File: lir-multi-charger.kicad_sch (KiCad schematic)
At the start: 2 parts, among them J1 Conn_01x02_Female

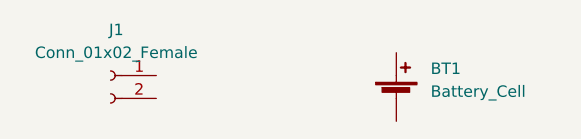
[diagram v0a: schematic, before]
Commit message: finished CR2450 battery holder footprint
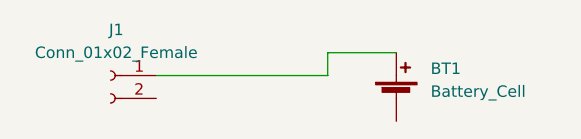
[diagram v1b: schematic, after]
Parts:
- BT1: footprint Battery:BatteryHolder_ComfortableElectronic_CH273-2450_1x2450 -> Battery_Coin_SMD:CR2450
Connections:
- net at BT1.1 (+): now also J1.1 (Pin_1)
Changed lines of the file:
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@@
 (kicad_sch (version 20211123) (generator eeschema)
   (paper "A4")
+  (wire (pts (xy 52.07 102.87) (xy 59.69 102.87))
+    (stroke (width 0) (type default) (color 0 0 0 0))
+  )
+  (wire (pts (xy 52.07 105.41) (xy 52.07 102.87))
+    (stroke (width 0) (type default) (color 0 0 0 0))
+  )
+  (wire (pts (xy 33.02 105.41) (xy 52.07 105.41))
+    (stroke (width 0) (type default) (color 0 0 0 0))
+  )
   (symbol (lib_id "Device:Battery_Cell") (at 59.69 107.95 0) (unit 1)
     (in_bom yes) (on_board yes) (fields_autoplaced)
@@
       (effects (font (size 1.27 1.27)) (justify left))
     )
-    (property "Footprint" "Battery:BatteryHolder_ComfortableElectronic_CH273-2450_1x2450" (id 2) (at 59.69 106.426 90)
+    (property "Footprint" "Battery_Coin_SMD:CR2450" (id 2) (at 59.69 106.426 90)
       (effects (font (size 1.27 1.27)) hide)
     )
@@
   (symbol_instances
     (path "/6a0c578b-7a8f-4b47-bae2-b91033c942ea"
-      (reference "BT1") (unit 1) (value "Battery_Cell") (footprint "Battery:BatteryHolder_ComfortableElectronic_CH273-2450_1x2450")
+      (reference "BT1") (unit 1) (value "Battery_Cell") (footprint "Battery_Coin_SMD:CR2450")
     )
     (path "/ecc76268-d1b1-479a-a89b-3a5c8226dd54"

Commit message: started charger schematic
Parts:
- removed J1: Conn_01x02_Female, TerminalBlock_4Ucon:TerminalBlock_4Ucon_1x02_P3.50mm_Horizontal, symbol Connector:Conn_01x02_Female
- added BT2: Battery_Cell, Battery_Coin_SMD:CR2032, symbol Device:Battery_Cell
- added BT3: Battery_Cell, Battery_Coin_SMD:CR1220, symbol Device:Battery_Cell
- added D1, D2: D_Schottky, Diode_SMD:D_SOD-123, symbol Device:D_Schottky
- added J1: USB_C_Receptacle_USB2.0, Connector_USB:USB_C_Receptacle_HRO_TYPE-C-31-M-12, symbol Connector:USB_C_Receptacle_USB2.0
- added J2: Conn_01x02_Male, Connector_PinHeader_2.54mm:PinHeader_1x02_P2.54mm_Vertical, symbol Connector:Conn_01x02_Male
- added R1, R2: 5.1K, Resistor_SMD:R_0805_2012Metric_Pad1.20x1.40mm_HandSolder, symbol Device:R
- added U1: TP4056, Package_SO:SOP-8_3.9x4.9mm_P1.27mm, symbol Li_ion_charger:TP4056
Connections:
- new net: D1.1 (K), D2.1 (K)
- new net: D1.2 (A), J2.1 (Pin_1)
- new net: J1.A5 (CC1), R2.1
- new net: D2.2 (A), J1.A4 (VBUS), J1.A9 (VBUS), J1.B4 (VBUS), J1.B9 (VBUS)
- new net: J1.A6 (D+), J1.B6 (D+)
- new net: J1.A7 (D-), J1.B7 (D-)
- new net: J1.B5 (CC2), R1.1
- new net GND: J1.A1 (GND), J1.A12 (GND), J1.B1 (GND), J1.B12 (GND), J2.2 (Pin_2), R1.2, R2.2
- no-connect marks 0 -> 3
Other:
- moved on the sheet: BT1

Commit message: started placing components
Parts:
- added C1, C2, C3, C4: 10uF, Capacitor_SMD:C_0805_2012Metric_Pad1.18x1.45mm_HandSolder, symbol Device:C
- added D3, D5: GREEN, LED_SMD:LED_0805_2012Metric_Pad1.15x1.40mm_HandSolder, symbol Device:LED
- added D4, D6: RED, LED_SMD:LED_0805_2012Metric_Pad1.15x1.40mm_HandSolder, symbol Device:LED
- added R10, R5: 0R, Resistor_SMD:R_0805_2012Metric_Pad1.20x1.40mm_HandSolder, symbol Device:R
- added R11, R6: 320k, Resistor_SMD:R_0805_2012Metric_Pad1.20x1.40mm_HandSolder, symbol Device:R
- added R12, R7: 1R, Resistor_SMD:R_0805_2012Metric_Pad1.20x1.40mm_HandSolder, symbol Device:R
- added R3, R4, R8, R9: 1k, Resistor_SMD:R_0805_2012Metric_Pad1.20x1.40mm_HandSolder, symbol Device:R
- added U2: TP4056, Li-ion-charger:tp4056, symbol Li_ion_charger:TP4056
- U1: footprint Package_SO:SOP-8_3.9x4.9mm_P1.27mm -> Li-ion-charger:tp4056
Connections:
- net GND: now also BT2.2 (-), BT3.2 (-), U1.1 (TEMP), U1.3 (GND), C1.2, C2.2, C3.2, C4.2, R12.2, R7.2, U2.1 (TEMP), U2.3 (GND)
- net VBUS: now reaches D1.1 (K), D2.1 (K)
- net VBUS: now also R10.1, R5.1
- net at BT2.1 (+): now also C4.1, U2.5 (BAT)
- net at BT3.1 (+): now also U1.5 (BAT), C2.1
- net at U1.2 (PROG): now also R6.1
- net at U1.4 (VCC): now also U1.8 (CE), C1.1, D3.2 (A), D4.2 (A), R5.2
- net at U1.6 (/STDBY): now also R4.2
- net at U1.7 (/CHRG): now also R3.2
- new net: D5.1 (K), R9.1
- new net: C3.1, D5.2 (A), D6.2 (A), R10.2, U2.4 (VCC), U2.8 (CE)
- new net: R9.2, U2.6 (/STDBY)
- new net: R11.1, U2.2 (PROG)
- new net: R11.2, R12.1
- new net: R6.2, R7.1
- new net: D4.1 (K), R3.1
- new net: D6.1 (K), R8.1
- new net: D3.1 (K), R4.1
- new net: R8.2, U2.7 (/CHRG)
- no-connect marks 3 -> 5
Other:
- moved on the sheet: BT1, BT2, BT3

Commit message: placing components
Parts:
- added C5, C6: 10uF, Capacitor_SMD:C_0805_2012Metric_Pad1.18x1.45mm_HandSolder, symbol Device:C
- added D7: GREEN, LED_SMD:LED_0805_2012Metric_Pad1.15x1.40mm_HandSolder, symbol Device:LED
- added D8: RED, LED_SMD:LED_0805_2012Metric_Pad1.15x1.40mm_HandSolder, symbol Device:LED
- added R13, R14: 1k, Resistor_SMD:R_0805_2012Metric_Pad1.20x1.40mm_HandSolder, symbol Device:R
- added R15: 0R, Resistor_SMD:R_0805_2012Metric_Pad1.20x1.40mm_HandSolder, symbol Device:R
- added R16: 320k, Resistor_SMD:R_0805_2012Metric_Pad1.20x1.40mm_HandSolder, symbol Device:R
- added R17: 1R, Resistor_SMD:R_0805_2012Metric_Pad1.20x1.40mm_HandSolder, symbol Device:R
- added U3: TP4056, Li-ion-charger:tp4056, symbol Li_ion_charger:TP4056
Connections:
- net GND: now also BT1.2 (-), C5.2, C6.2, R17.2, U3.1 (TEMP), U3.3 (GND)
- net VBUS: now also R15.1
- net at BT1.1 (+): now also C6.1, U3.5 (BAT)
- new net: R16.1, U3.2 (PROG)
- new net: C5.1, D7.2 (A), D8.2 (A), R15.2, U3.4 (VCC), U3.8 (CE)
- new net: R14.2, U3.6 (/STDBY)
- new net: R13.2, U3.7 (/CHRG)
- new net: D8.1 (K), R13.1
- new net: D7.1 (K), R14.1
- new net: R16.2, R17.1
- no-connect marks 5 -> 6
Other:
- moved on the sheet: BT1, BT2, BT3, C1, C2, C3, C4, D3, D4, D5, D6, R10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

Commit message: all components placed
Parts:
- added J3, J4, J5, J6: Conn_01x02_Male, Connector_PinHeader_2.54mm:PinHeader_1x02_P2.54mm_Vertical, symbol Connector:Conn_01x02_Male
- added JP1, JP2, JP3: SolderJumper_2_Bridged, Jumper:SolderJumper-2_P1.3mm_Bridged_RoundedPad1.0x1.5mm, symbol Jumper:SolderJumper_2_Bridged
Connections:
- net at C6.1, U3.5 (BAT): now also J5.1 (Pin_1), JP3.1 (A); no longer BT1.1 (+)
- net at C2.1, U1.5 (BAT): now also J3.1 (Pin_1), JP1.1 (A); no longer BT3.1 (+)
- net at C4.1, U2.5 (BAT): now also J4.1 (Pin_1), JP2.1 (A); no longer BT2.1 (+)
- net at J1.A6 (D+), J1.B6 (D+): now also J6.1 (Pin_1)
- net at J1.A7 (D-), J1.B7 (D-): now also J6.2 (Pin_2)
- new net: BT1.1 (+), J5.2 (Pin_2), JP3.2 (B)
- new net: BT2.1 (+), J4.2 (Pin_2), JP2.2 (B)
- new net: BT3.1 (+), J3.2 (Pin_2), JP1.2 (B)
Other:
- moved on the sheet: BT1, R1, R2

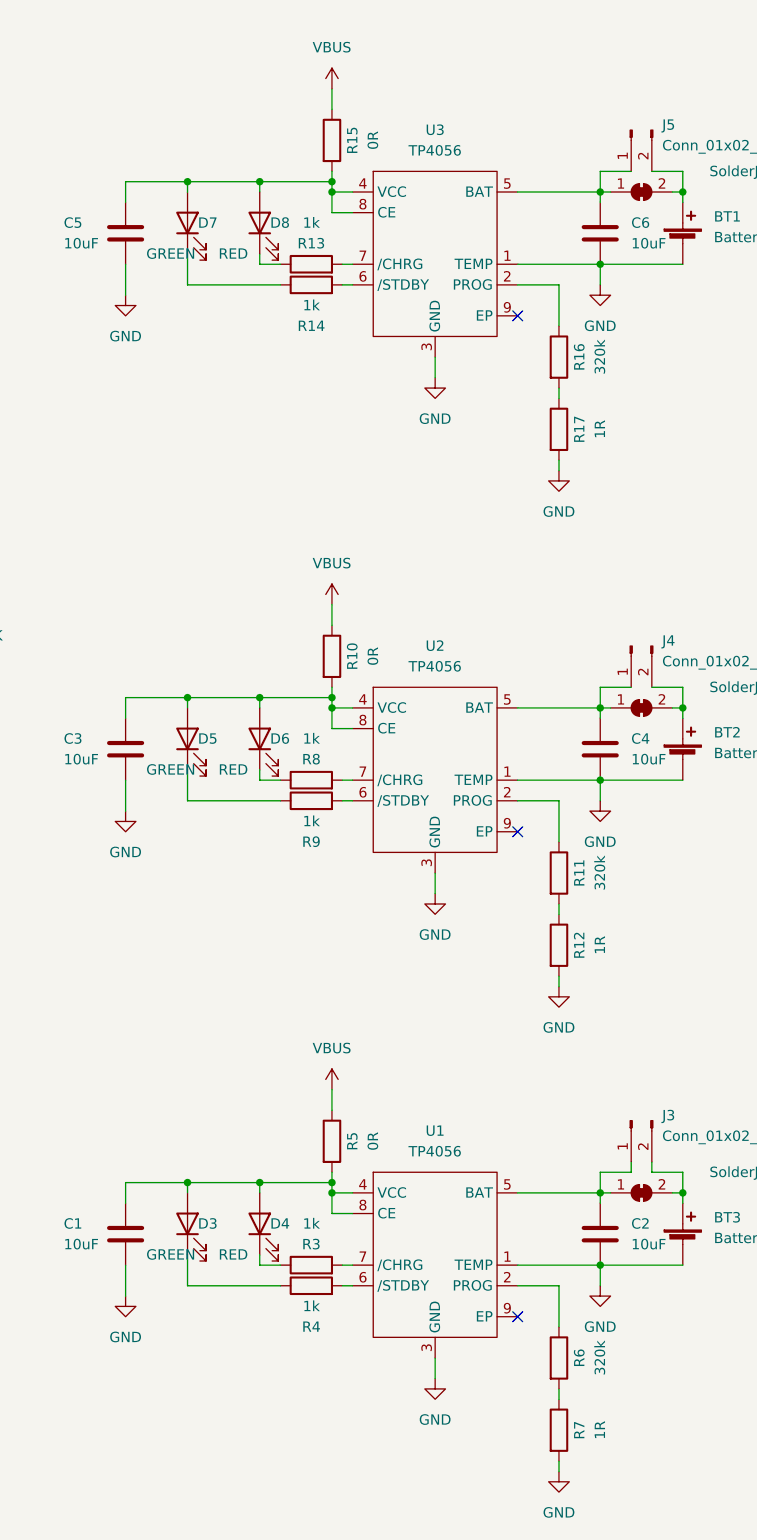
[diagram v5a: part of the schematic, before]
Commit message: changed charger IC
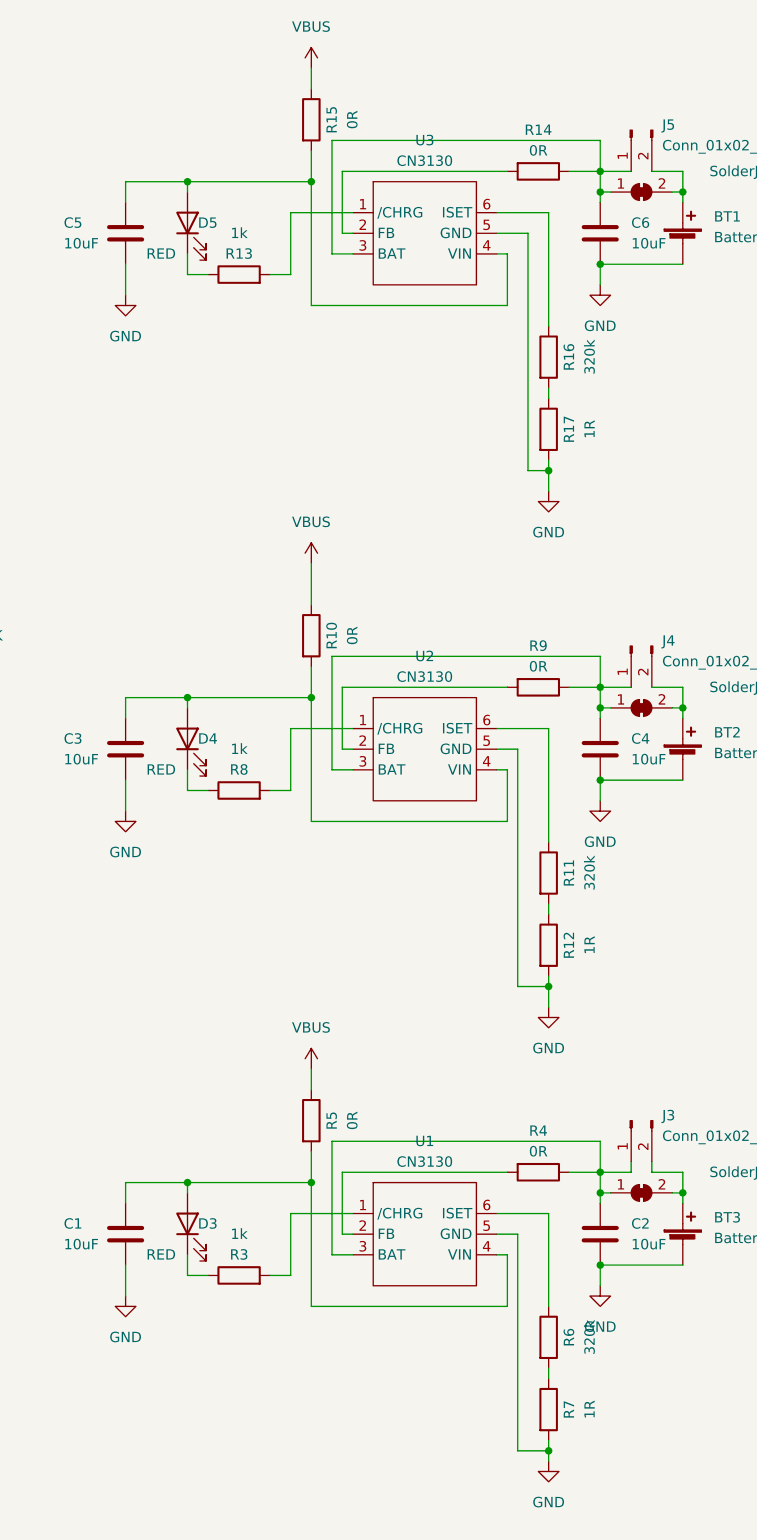
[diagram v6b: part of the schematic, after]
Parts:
- removed D3, D5, D7: GREEN, LED_SMD:LED_0805_2012Metric_Pad1.15x1.40mm_HandSolder, symbol Device:LED
- removed U1, U2, U3: TP4056, Li-ion-charger:tp4056, symbol Li_ion_charger:TP4056
- added U1, U2, U3: CN3130, Package_TO_SOT_SMD:SOT-23-6_Handsoldering, symbol coin-batt-charger:CN3130
- R14, R4, R9: value 1k -> 0R
- renumbered D4 to D3, D6 to D4, D8 to D5
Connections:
- net GND: now also U1.5 (GND), U2.5 (GND), U3.5 (GND)
- net at R16.1: now also U3.6 (ISET)
- net at C5.1, D5.2 (A), R15.2: now also U3.4 (VIN)
- net at C6.1, J5.1 (Pin_1), JP3.1 (A): now also R14.1, U3.3 (BAT)
- net at R14.2: now also U3.2 (FB)
- net at R13.2: now also U3.1 (/CHRG)
- net at R9.1: now also C4.1, J4.1 (Pin_1), JP2.1 (A), U2.3 (BAT)
- net at C3.1, D4.2 (A), R10.2: now also U2.4 (VIN)
- net at R9.2: now also U2.2 (FB)
- net at C1.1, D3.2 (A), R5.2: now also U1.4 (VIN)
- net at R6.1: now also U1.6 (ISET)
- net at C2.1, J3.1 (Pin_1), JP1.1 (A): now also R4.1, U1.3 (BAT)
- net at R4.2: now also U1.2 (FB)
- net at R3.2: now also U1.1 (/CHRG)
- net at R11.1: now also U2.6 (ISET)
- net at R8.2: now also U2.1 (/CHRG)
- no-connect marks 6 -> 3
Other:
- moved on the sheet: D3, D4, D5, R10, R11, R12, R13, R15, R16, R17, R3, R5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

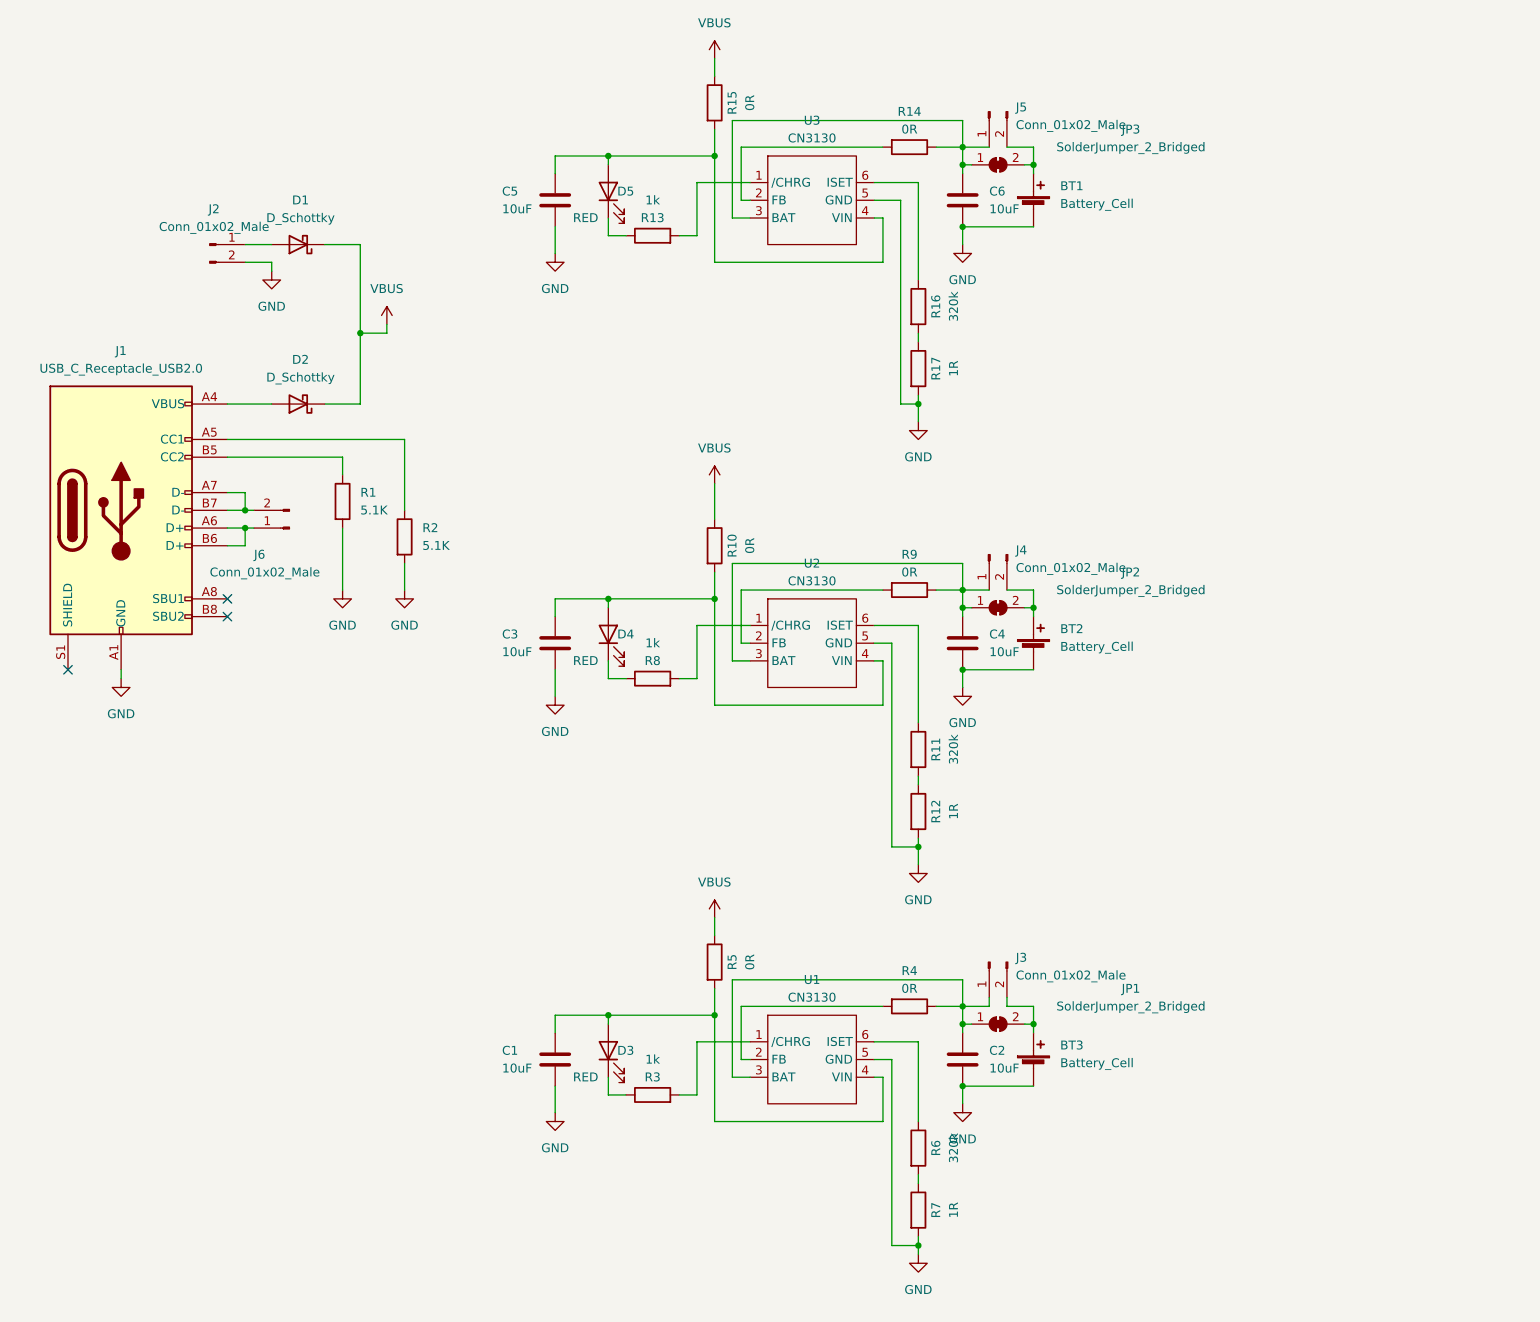
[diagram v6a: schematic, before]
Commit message: upgraded kicad version to 9, starting to add ext bat connectors
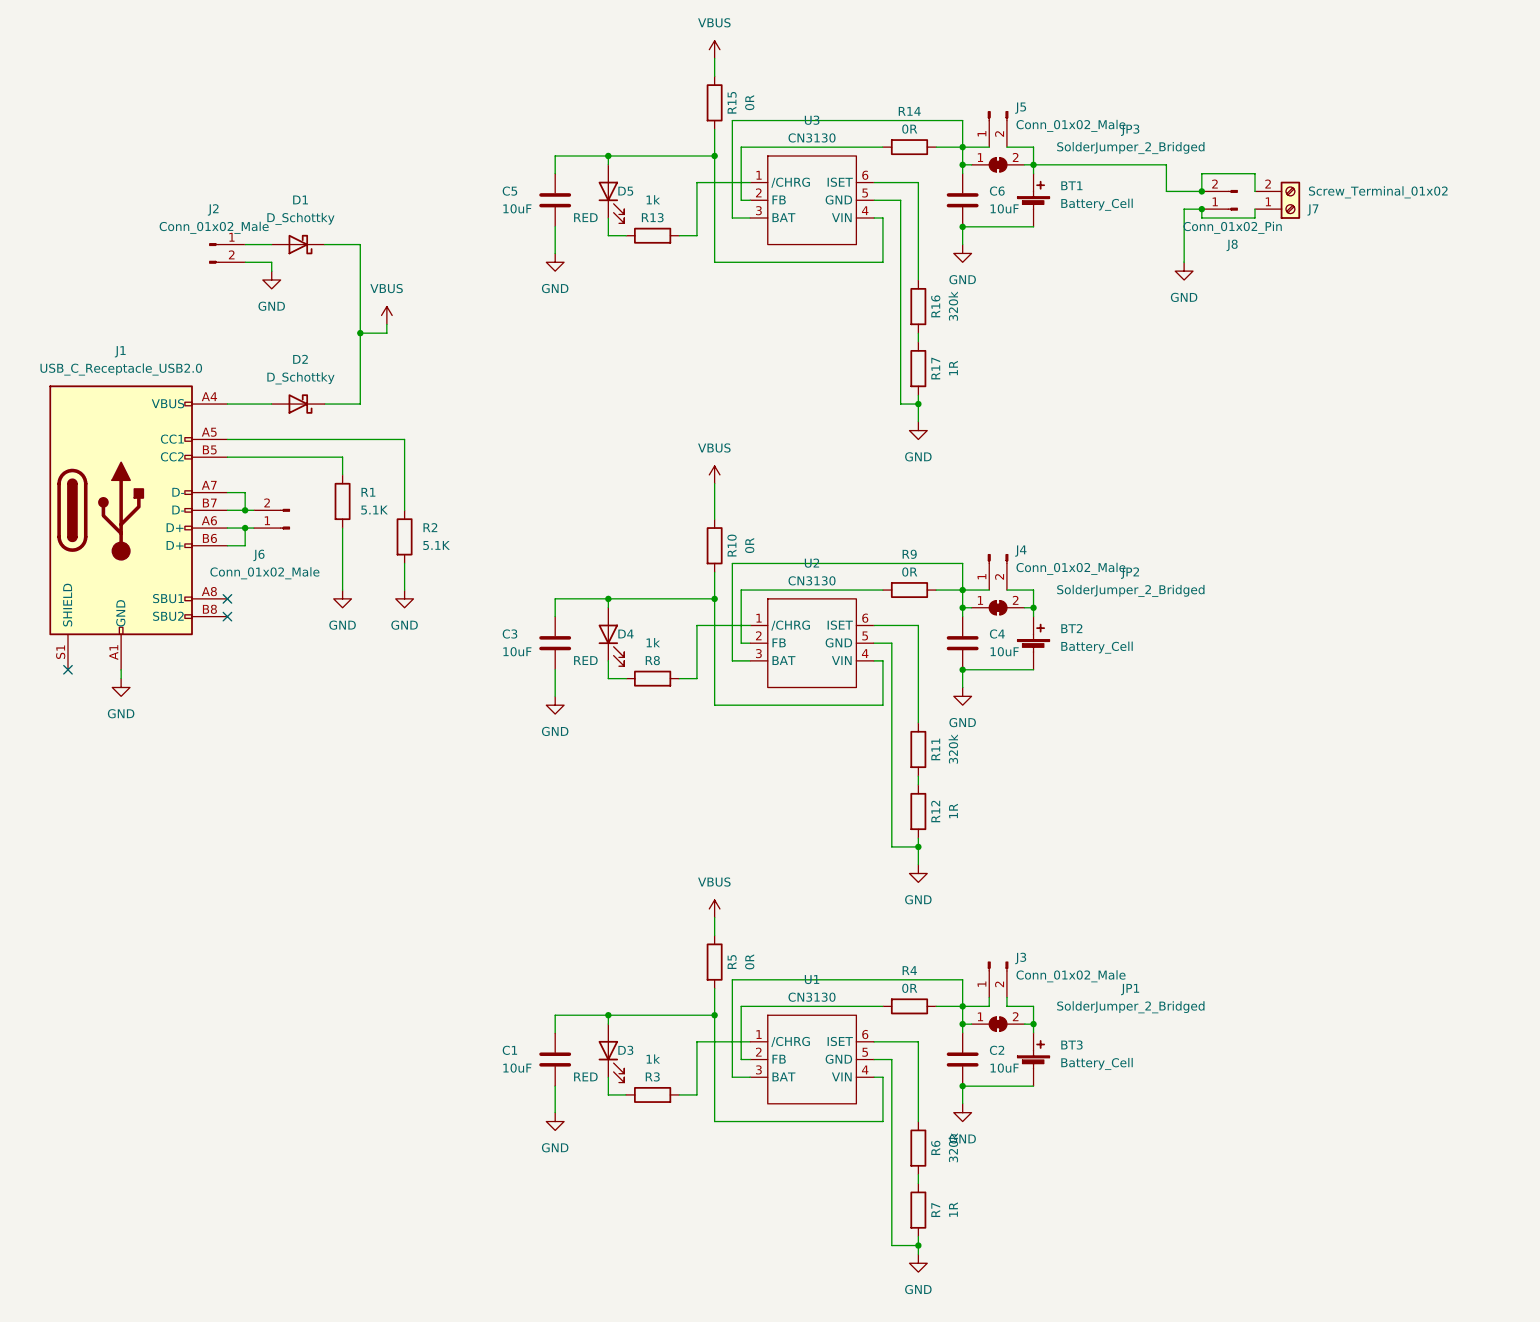
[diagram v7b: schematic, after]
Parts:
- added J7: Screw_Terminal_01x02, TerminalBlock_4Ucon:TerminalBlock_4Ucon_1x02_P3.50mm_Horizontal, symbol Connector:Screw_Terminal_01x02
- added J8: Conn_01x02_Pin, Connector_PinHeader_2.54mm:PinHeader_1x02_P2.54mm_Vertical, symbol Connector:Conn_01x02_Pin
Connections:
- net GND: now also J7.1 (Pin_1), J8.1 (Pin_1)
- net at BT1.1 (+), J5.2 (Pin_2), JP3.2 (B): now also J7.2 (Pin_2), J8.2 (Pin_2)
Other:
- title: (none) -> LIR-MULTI-CHARGER
